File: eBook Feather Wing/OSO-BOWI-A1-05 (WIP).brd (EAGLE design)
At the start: 77.5 x 112.3 mm, 100 parts, among them IC1 MCP23008/SO, IC2 23K256-I/SN, J1 SJ-43514-SMT, Q1 IRLML0100, SW1 SPDT_SWITCH

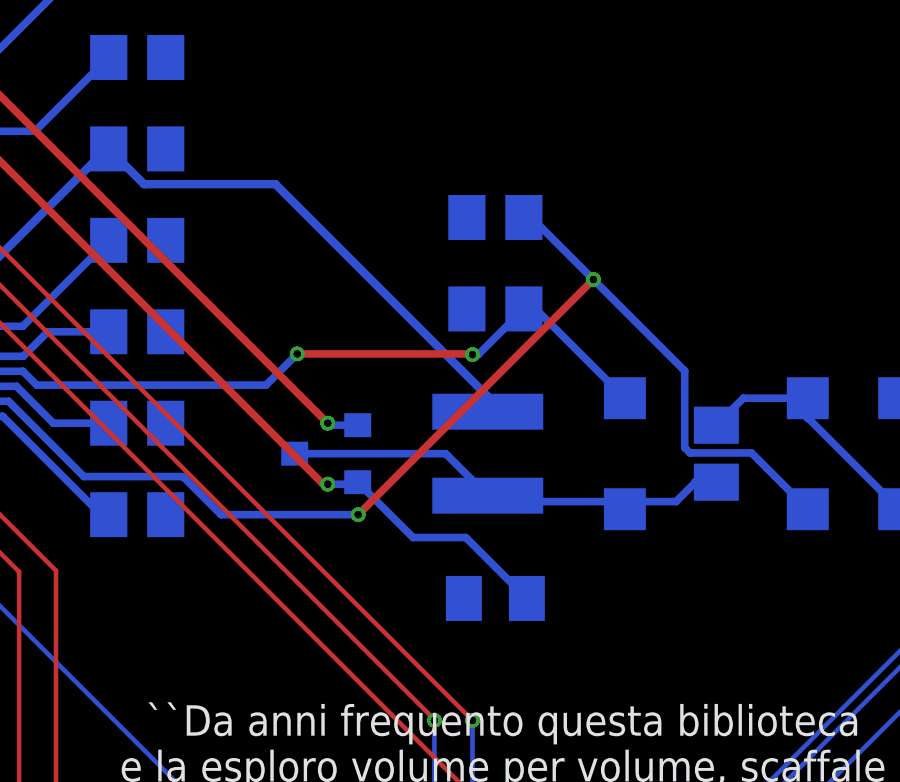
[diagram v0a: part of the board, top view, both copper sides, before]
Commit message: wing: new footprint for inductor
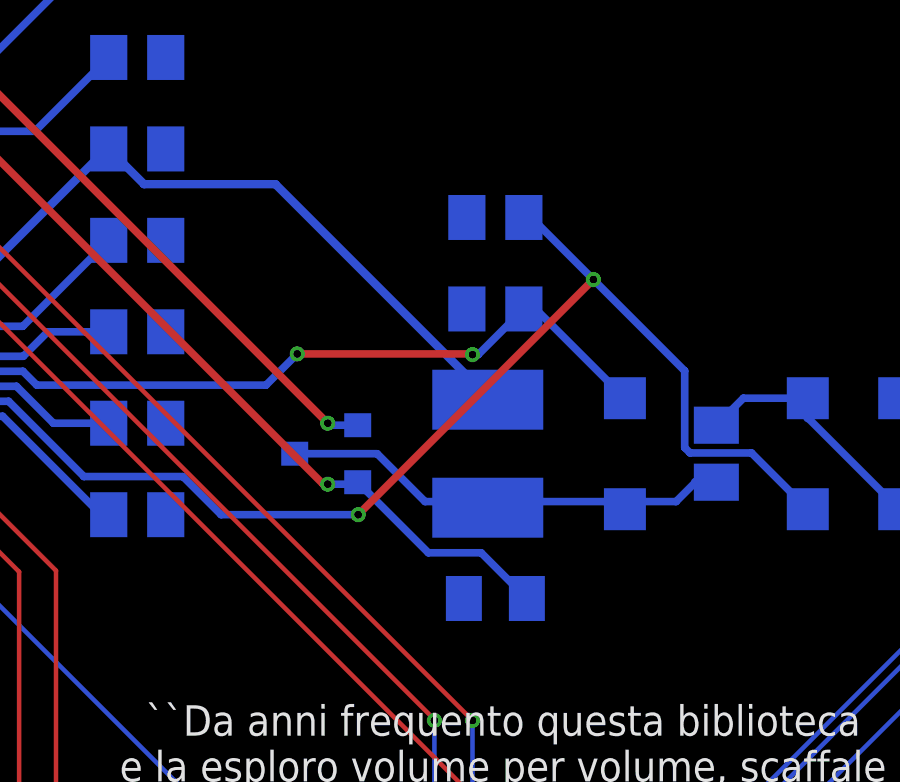
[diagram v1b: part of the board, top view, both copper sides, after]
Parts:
- L1: device microbuilder:INDUCTOR_4X4MM_NR401 -> Adafruit 3.5in 480x320 FeatherWing:MICROBUILDER_INDUCTOR_4X4MM_NR401_BIGPADS
- turned L1 to 270 degrees
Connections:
- net +3V3: now also L1.P$1; no longer L1.P$2
- net N$3: now also L1.P$2; no longer L1.P$1
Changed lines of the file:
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@@
 <attribute name="VALUE" x="44.45" y="78.486" size="0.508" layer="28" font="vector" ratio="18" rot="MR270" align="center"/>
-</element>
-<element name="L1" library="microbuilder" package="INDUCTOR_4X4MM_NR401" value="10uH" x="38.1" y="77.216" smashed="yes" rot="MR90">
-<attribute name="NAME" x="38.1" y="74.676" size="0.508" layer="26" font="vector" ratio="18" rot="MR0" align="center"/>
-<attribute name="VALUE" x="41.3" y="75.216" size="0.508" layer="28" font="vector" ratio="18" rot="MR90" align="center"/>
 </element>
 <element name="R5" library="microbuilder" package="0805_10MGAP" value="0.47ohm" x="38.354" y="72.39" smashed="yes" rot="MR0">
@@
 <attribute name="NAME" x="66.0082" y="107.9642" size="0.8128" layer="26" ratio="18" rot="MR180"/>
 <attribute name="VALUE" x="66.0082" y="108.9142" size="0.4064" layer="28" ratio="10" rot="MR180"/>
+</element>
+<element name="L1" library="Adafruit 3.5in 480x320 FeatherWing" package="MICROBUILDER_INDUCTOR_4X4MM_NR401_BIGPADS" value="10uH" x="38.1" y="77.216" smashed="yes" rot="MR270">
+<attribute name="NAME" x="38.1" y="73.914" size="0.508" layer="26" font="vector" ratio="18" rot="MR0" align="center"/>
+<attribute name="VALUE" x="34.9" y="79.216" size="0.8128" layer="28" ratio="12" rot="MR270"/>
 </element>
 </elements>
@@
 <contactref element="MS1" pad="2"/>
 <contactref element="MS1" pad="2'"/>
-<contactref element="L1" pad="P$2"/>
 <contactref element="U$2" pad="15"/>
 <contactref element="C12" pad="2"/>
@@
 <wire x1="20.4874" y1="82.4634" x2="17.6532" y2="82.4634" width="0.2794" layer="16"/>
 <wire x1="17.6532" y1="82.9634" x2="20.9874" y2="82.9634" width="0.2794" layer="16"/>
-<wire x1="38.1" y1="79.124" x2="38.1" y2="78.616" width="0.2794" layer="16"/>
 <wire x1="72.672" y1="22.987" x2="67.945" y2="22.987" width="0.3048" layer="16"/>
 <wire x1="53.848" y1="8.89" x2="48.006" y2="8.89" width="0.3048" layer="16"/>
@@
 <wire x1="25.466" y1="87.376" x2="26.642" y2="86.2" width="0.2794" layer="16"/>
 <wire x1="31.024" y1="86.2" x2="26.642" y2="86.2" width="0.2794" layer="16"/>
-<wire x1="31.024" y1="86.2" x2="38.1" y2="79.124" width="0.2794" layer="16"/>
+<wire x1="38.1" y1="79.124" x2="31.024" y2="86.2" width="0.2794" layer="16"/>
 <wire x1="25.4" y1="87.376" x2="25.466" y2="87.376" width="0.3048" layer="16"/>
 <via x="19.812" y="20.32" extent="1-16" drill="0.254"/>
@@
 <wire x1="48.006" y1="8.89" x2="46.6598" y2="8.89" width="0.6096" layer="16"/>
 <wire x1="46.6598" y1="8.89" x2="46.228" y2="8.4582" width="0.6096" layer="16"/>
+<contactref element="L1" pad="P$1"/>
+<wire x1="38.1" y1="79.016" x2="38.1" y2="79.124" width="0.254" layer="16"/>
 </signal>
 <signal name="GDR">
@@
 <wire x1="19.57235" y1="89.24125" x2="19.2945" y2="88.9634" width="0.254" layer="16"/>
 <wire x1="19.2945" y1="88.9634" x2="17.6532" y2="88.9634" width="0.254" layer="16"/>
-<wire x1="37.372" y1="74.422" x2="39.404" y2="72.39" width="0.254" layer="16"/>
-<wire x1="37.372" y1="74.422" x2="35.61" y2="74.422" width="0.254" layer="16"/>
-<wire x1="35.61" y1="74.422" x2="33.766" y2="76.266" width="0.254" layer="16"/>
+<wire x1="37.88" y1="73.914" x2="39.404" y2="72.39" width="0.254" layer="16"/>
+<wire x1="37.88" y1="73.914" x2="36.118" y2="73.914" width="0.254" layer="16"/>
+<wire x1="36.118" y1="73.914" x2="33.766" y2="76.266" width="0.254" layer="16"/>
 </signal>
 <signal name="VCOM">
@@
 <signal name="N$3">
 <contactref element="D3" pad="A"/>
-<contactref element="L1" pad="P$1"/>
 <contactref element="Q1" pad="3"/>
 <contactref element="C9" pad="1"/>
 <wire x1="45.024" y1="76.266" x2="45.72" y2="76.266" width="0.3048" layer="16"/>
 <wire x1="45.024" y1="76.266" x2="44.378" y2="75.62" width="0.254" layer="16"/>
-<wire x1="36.7" y1="77.216" x2="31.666" y2="77.216" width="0.254" layer="16"/>
-<wire x1="38.296" y1="75.62" x2="42.672" y2="75.62" width="0.254" layer="16"/>
+<wire x1="31.666" y1="77.216" x2="34.414" y2="77.216" width="0.254" layer="16"/>
+<wire x1="42.672" y1="75.62" x2="38.296" y2="75.62" width="0.254" layer="16"/>
+<wire x1="38.296" y1="75.62" x2="36.01" y2="75.62" width="0.254" layer="16"/>
 <wire x1="44.378" y1="75.62" x2="42.672" y2="75.62" width="0.254" layer="16"/>
 <wire x1="42.672" y1="75.366" x2="42.672" y2="75.62" width="0.3048" layer="16"/>
-<wire x1="38.1" y1="75.816" x2="36.7" y2="77.216" width="0.254" layer="16"/>
-<wire x1="38.1" y1="75.816" x2="38.296" y2="75.62" width="0.3048" layer="16"/>
+<contactref element="L1" pad="P$2"/>
+<wire x1="34.414" y1="77.216" x2="36.01" y2="75.62" width="0.254" layer="16"/>
+<wire x1="38.1" y1="75.416" x2="38.1" y2="75.424" width="0.254" layer="16"/>
+<wire x1="38.1" y1="75.424" x2="38.296" y2="75.62" width="0.254" layer="16"/>
 </signal>
 <signal name="EINK_RESET">
